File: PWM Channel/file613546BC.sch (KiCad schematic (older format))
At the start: 8 parts, among them U201 NE555P

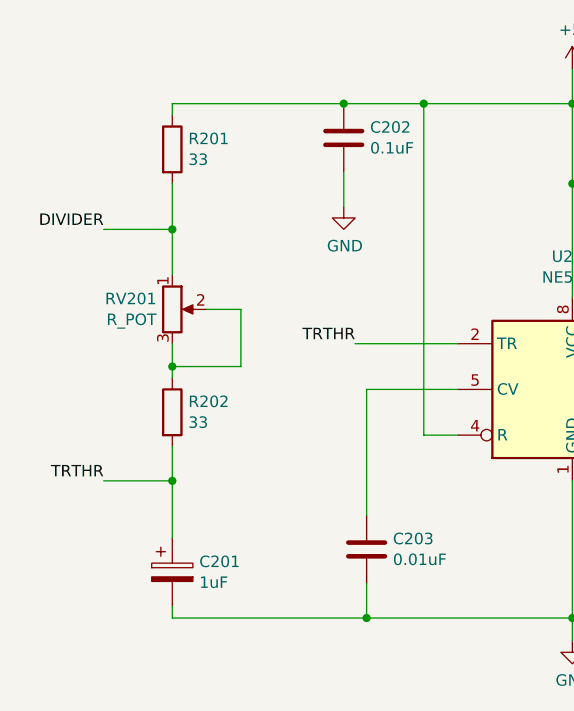
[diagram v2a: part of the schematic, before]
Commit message: Rerouting everything
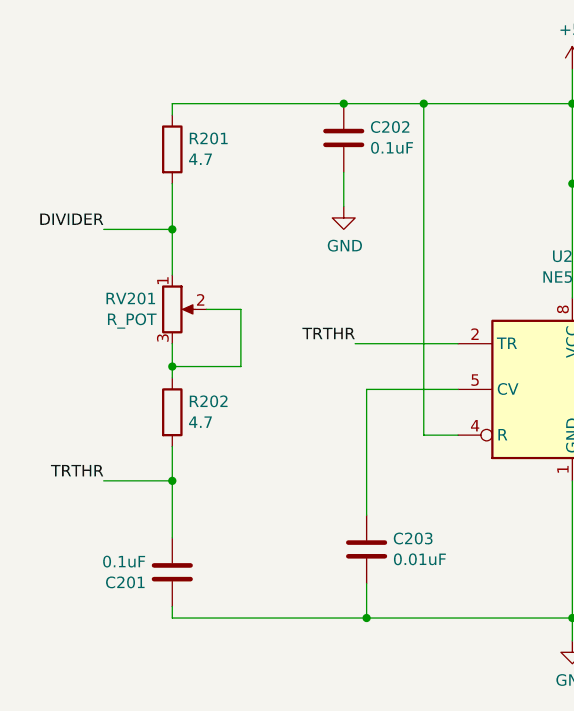
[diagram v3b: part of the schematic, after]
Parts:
- removed C201: 1uF, Capacitor_THT:CP_Radial_D4.0mm_P1.50mm, symbol Device:CP
- added C201: 0.1uF, Capacitor_THT:C_Disc_D4.3mm_W1.9mm_P5.00mm, symbol Device:C
- R201, R202: value 33 -> 4.7
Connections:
- net GND: now also C201.2
- net TRTHR: now also C201.1
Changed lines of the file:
@@
 Wire Wire Line
 	3250 3400 3250 3500
-$Comp
-L Device:CP C201
-U 1 1 60265318
-P 1500 3200
-F 0 "C201" H 1618 3246 50  0000 L CNN
-F 1 "1uF" H 1618 3155 50  0000 L CNN
-F 2 "Capacitor_THT:CP_Radial_D4.0mm_P1.50mm" H 1538 3050 50  0001 C CNN
-F 3 "~" H 1500 3200 50  0001 C CNN
-	1    1500 3200
-	1    0    0    -1
-$EndComp
 Wire Wire Line
 	2350 3400 1500 3400
@@
 P 1500 2500
 F 0 "R202" H 1570 2546 50  0000 L CNN
-F 1 "33" H 1570 2455 50  0000 L CNN
+F 1 "4.7" H 1570 2455 50  0000 L CNN
 F 2 "Resistor_THT:R_Axial_DIN0207_L6.3mm_D2.5mm_P7.62mm_Horizontal" V 1430 2500 50  0001 C CNN
 F 3 "~" H 1500 2500 50  0001 C CNN
@@
 P 1500 1350
 F 0 "R201" H 1570 1396 50  0000 L CNN
-F 1 "33" H 1570 1305 50  0000 L CNN
+F 1 "4.7" H 1570 1305 50  0000 L CNN
 F 2 "Resistor_THT:R_Axial_DIN0207_L6.3mm_D2.5mm_P7.62mm_Horizontal" V 1430 1350 50  0001 C CNN
 F 3 "~" H 1500 1350 50  0001 C CNN
@@
 Wire Wire Line
 	1500 1150 1500 1200
+$Comp
+L Device:C C201
+U 1 1 61358D9F
+P 1500 3200
+F 0 "C201" H 1385 3154 50  0000 R CNN
+F 1 "0.1uF" H 1385 3245 50  0000 R CNN
+F 2 "Capacitor_THT:C_Disc_D4.3mm_W1.9mm_P5.00mm" H 1538 3050 50  0001 C CNN
+F 3 "~" H 1500 3200 50  0001 C CNN
+	1    1500 3200
+	1    0    0    -1
+$EndComp
 $EndSCHEMATC

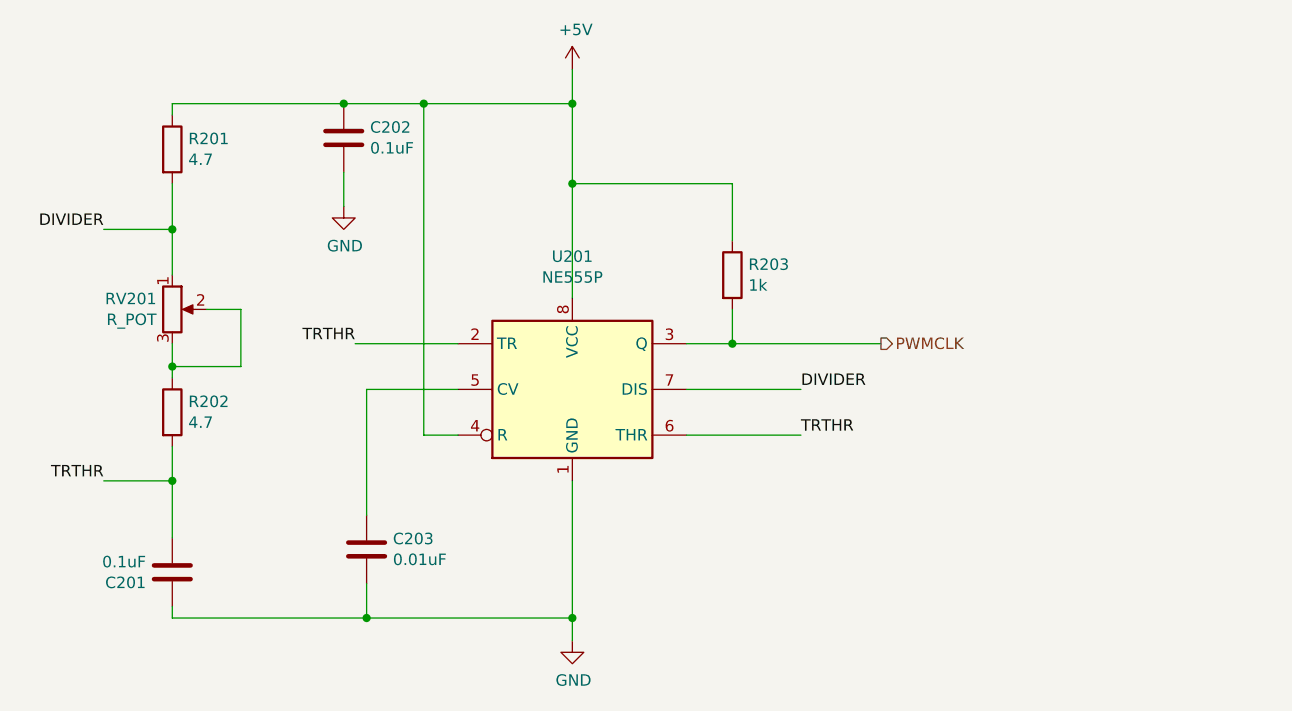
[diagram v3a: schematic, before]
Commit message: Updates to PWM Channel Board (#6)
Add a number of LED indicators and reduce from 12-bit to 8-bit
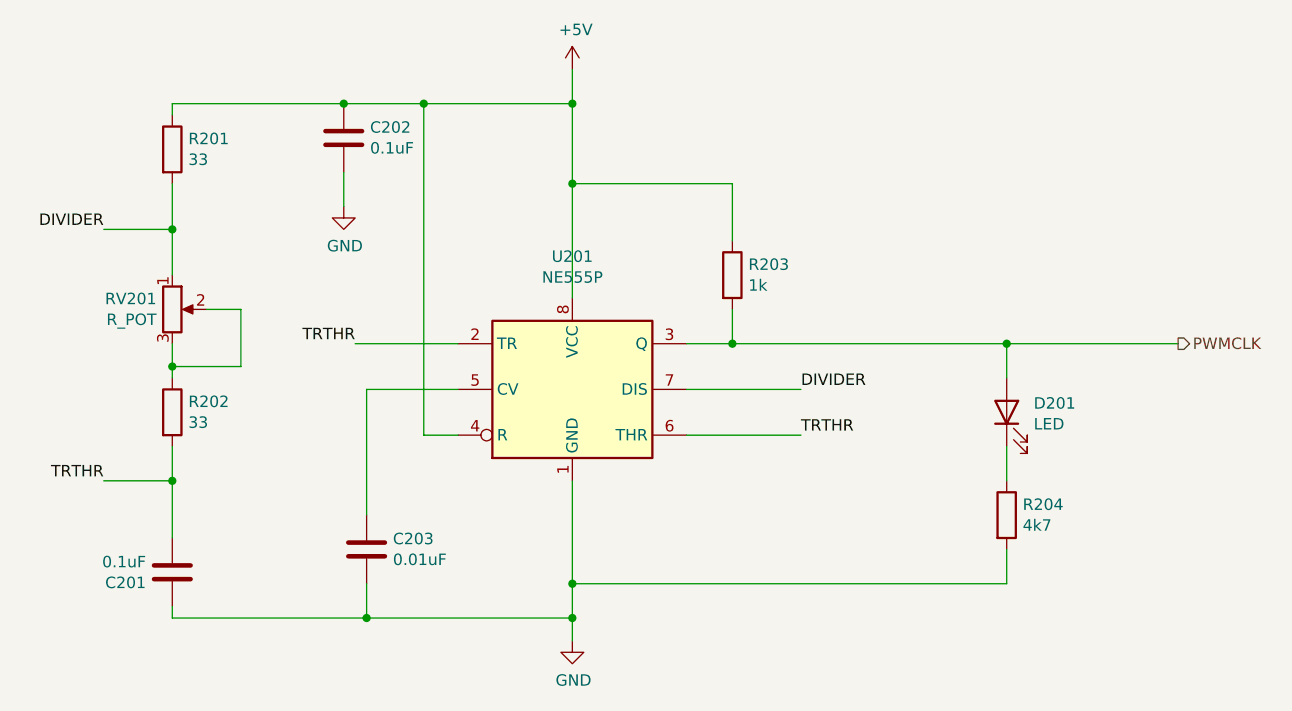
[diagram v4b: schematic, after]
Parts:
- added D201: LED, LED_THT:LED_D3.0mm, symbol Device:LED
- added R204: 4k7, Resistor_THT:R_Axial_DIN0207_L6.3mm_D2.5mm_P7.62mm_Horizontal, symbol Device:R
- R201, R202: value 4.7 -> 33
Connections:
- net GND: now also R204.2
- net PWMCLK: now also D201.2 (A)
- new net: D201.1 (K), R204.1
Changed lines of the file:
@@
 	3250 2000 3250 1500
 Wire Wire Line
-	3250 2800 3250 3400
+	3250 2800 3250 3250
 Wire Wire Line
 	2250 1150 2600 1150
@@
 P 1500 2500
 F 0 "R202" H 1570 2546 50  0000 L CNN
-F 1 "4.7" H 1570 2455 50  0000 L CNN
+F 1 "33" H 1570 2455 50  0000 L CNN
 F 2 "Resistor_THT:R_Axial_DIN0207_L6.3mm_D2.5mm_P7.62mm_Horizontal" V 1430 2500 50  0001 C CNN
 F 3 "~" H 1500 2500 50  0001 C CNN
@@
 P 1500 1350
 F 0 "R201" H 1570 1396 50  0000 L CNN
-F 1 "4.7" H 1570 1305 50  0000 L CNN
+F 1 "33" H 1570 1305 50  0000 L CNN
 F 2 "Resistor_THT:R_Axial_DIN0207_L6.3mm_D2.5mm_P7.62mm_Horizontal" V 1430 1350 50  0001 C CNN
 F 3 "~" H 1500 1350 50  0001 C CNN
@@
 Wire Wire Line
 	3750 2400 4250 2400
-Wire Wire Line
-	3950 2200 4600 2200
 Connection ~ 3950 2200
-Text HLabel 4600 2200 2    50   Output ~ 0
+Text HLabel 5900 2200 2    50   Output ~ 0
 PWMCLK
 $Comp
@@
 	1500 1150 1500 1200
 $Comp
+L Device:LED D?
+U 1 1 6163F56D
+P 5150 2500
+AR Path="/613636AA/6163F56D" Ref="D?"  Part="1"
+AR Path="/613546BD/6163F56D" Ref="D201"  Part="1"
+F 0 "D201" V 5189 2382 50  0000 R CNN
+F 1 "LED" V 5098 2382 50  0000 R CNN
+F 2 "LED_THT:LED_D3.0mm" H 5150 2500 50  0001 C CNN
+F 3 "~" H 5150 2500 50  0001 C CNN
+	1    5150 2500
+	0    -1   -1   0
+$EndComp
+$Comp
+L Device:R R?
+U 1 1 6163F573
+P 5150 2950
+AR Path="/613636AA/6163F573" Ref="R?"  Part="1"
+AR Path="/613546BD/6163F573" Ref="R204"  Part="1"
+F 0 "R204" H 5220 2996 50  0000 L CNN
+F 1 "4k7" H 5220 2905 50  0000 L CNN
+F 2 "Resistor_THT:R_Axial_DIN0207_L6.3mm_D2.5mm_P7.62mm_Horizontal" V 5080 2950 50  0001 C CNN
+F 3 "~" H 5150 2950 50  0001 C CNN
+	1    5150 2950
+	1    0    0    -1
+$EndComp
+Wire Wire Line
+	3950 2200 5150 2200
+Wire Wire Line
+	5150 2200 5150 2350
+Connection ~ 5150 2200
+Wire Wire Line
+	5150 2200 5900 2200
+Wire Wire Line
+	5150 2650 5150 2800
+Wire Wire Line
+	5150 3100 5150 3250
+Wire Wire Line
+	5150 3250 3250 3250
+Connection ~ 3250 3250
+Wire Wire Line
+	3250 3250 3250 3400
+$Comp
 L Device:C C201
-U 1 1 61358D9F
+U 1 1 616B46B5
 P 1500 3200
 F 0 "C201" H 1385 3154 50  0000 R CNN
